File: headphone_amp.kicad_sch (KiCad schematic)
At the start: 0 parts

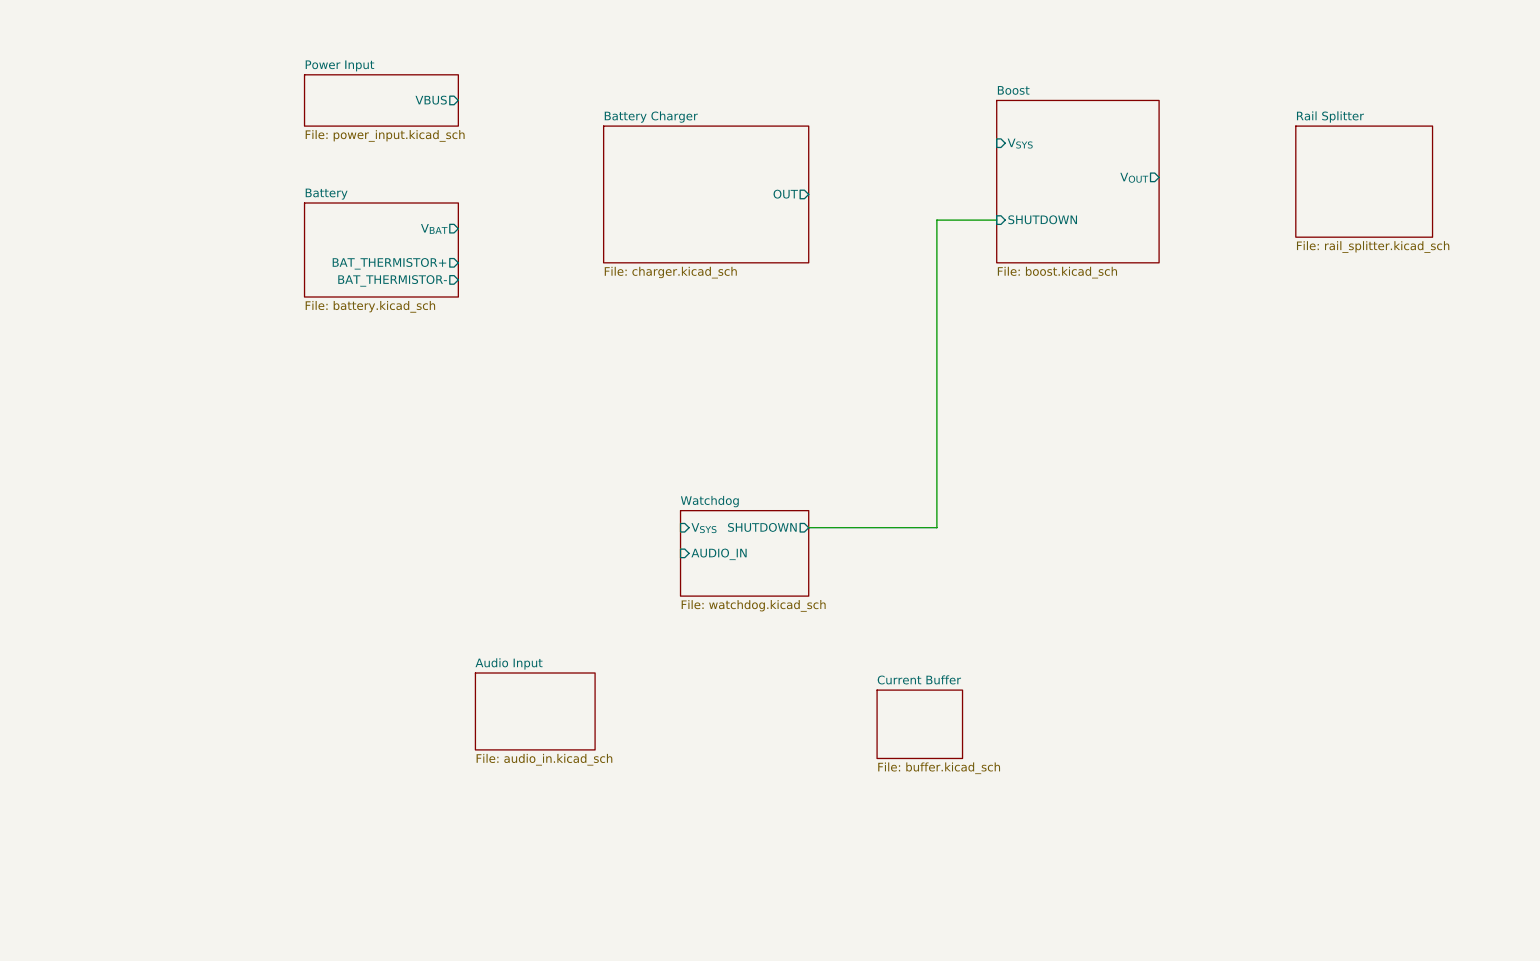
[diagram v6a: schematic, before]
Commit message: First rough draft of schematics complete -- missing a lot of PLM/Inventree work. Ran through several Claude reviews.
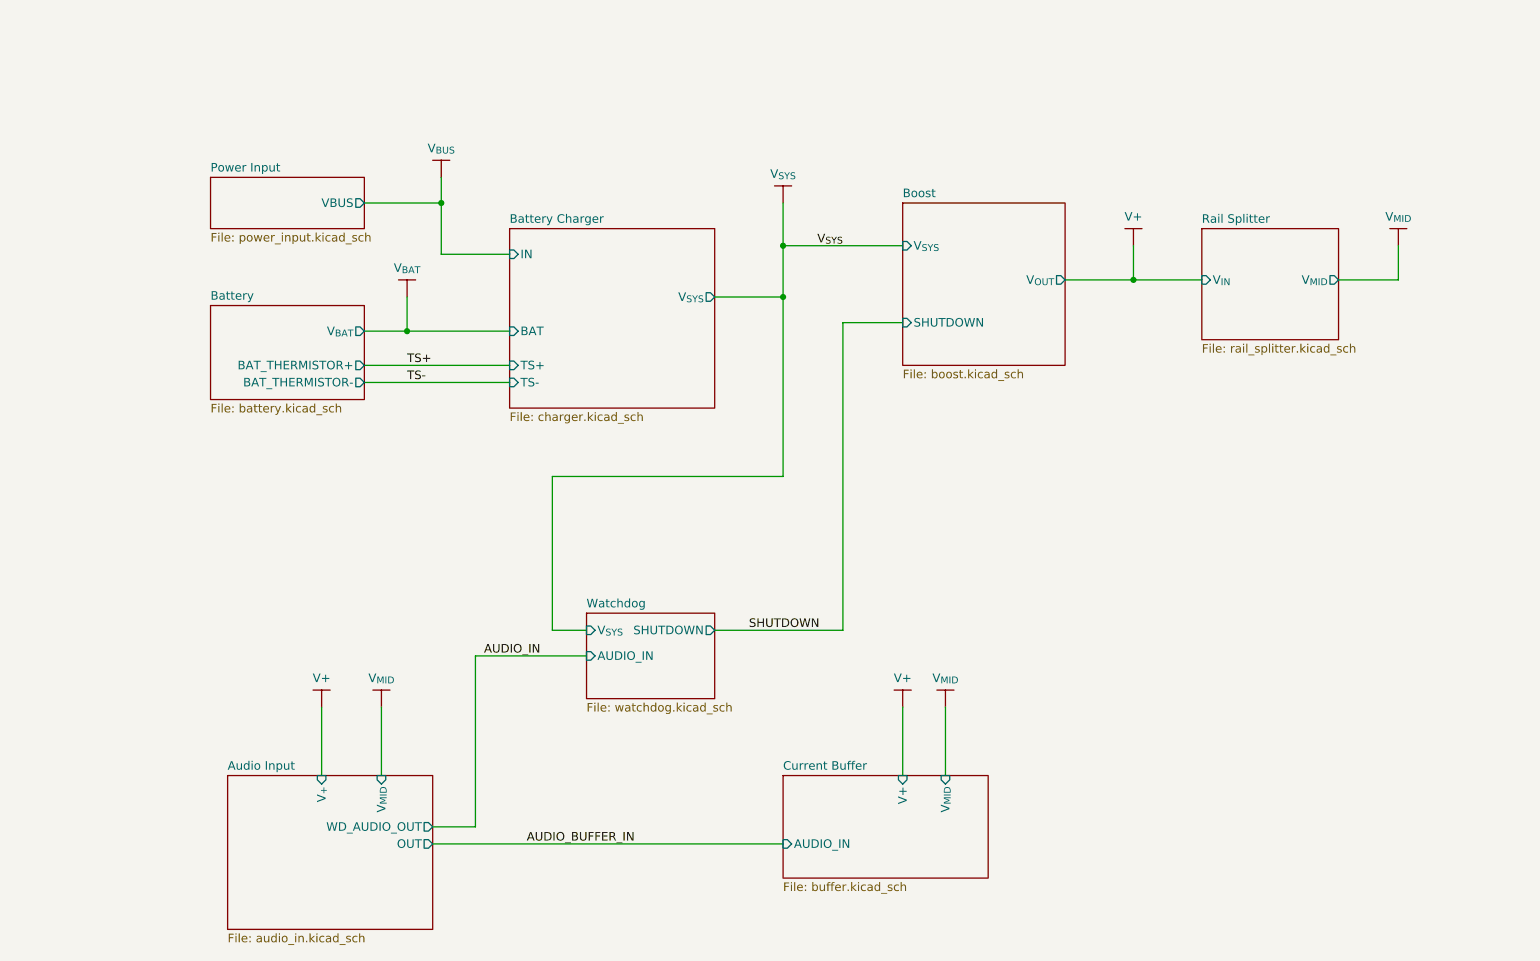
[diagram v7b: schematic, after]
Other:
- sheet Audio Input ports: added OUT, V_{+}, V_{MID}, WD_AUDIO_OUT; removed none
- sheet Battery Charger ports: added BAT, IN, TS+, TS-, V_{SYS}; removed OUT
- sheet Current Buffer ports: added AUDIO_IN, V+, V_{MID}; removed none
- sheet Rail Splitter ports: added V_{IN}, V_{MID}; removed none
